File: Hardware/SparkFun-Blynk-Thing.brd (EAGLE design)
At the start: 50.2 x 41.9 mm, 100 parts, among them Q1 MMBT2222A, Q2 MMBT2222A, Q3 2.5A/30V, U2 ESP8266, U3 W25Q32FVSS, U4 FT231XS-U, U5 SI7021, U6 MCP73831, U7 AP2112K-3.3V, U8 OPAMP-DUALU, Y1 26MHz

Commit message: Schematic cleanup
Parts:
- removed C19: 2.2uF, SparkFun-Capacitors:0603-CAP
- removed D7: RED, SparkFun-LED:LED-0603
- removed J1, J10, J12, J5, J7, J8, J9: (no value), blynk-thing-temp:1X01_ALLIGATOR_3MM_HALF
- removed R22: 2.0k, SparkFun-Resistors:0603-RES
- removed R25: 22K, SparkFun-Resistors:0603-RES
- removed R26: 10K, SparkFun-Resistors:0603-RES
- removed U7: AP2112K-3.3V, SparkFun-PowerIC:SOT23-5
- added C5: 0.1uF, SparkFun-Capacitors:0603-CAP
- added D2: BAT20J, SparkFun-DiscreteSemi:SOD-323
- added JP19, JP21, JP23, JP25, JP27, JP28: (no value), SparkFun-Connectors:1X01_NO_SILK
- added JP29: (no value), SparkFun-Connectors:JST-4-PTH-VERT
- added R11: 330, SparkFun-Resistors:0603-RES
- added R13: 27, SparkFun-Resistors:0603-RES
- added R15: 4.7K, SparkFun-Resistors:0603-RES
- added U1: MCP73831, SparkFun-PowerIC:SOT23-5
- C10: value 0.1uF -> 2.2uF
- C11, C9: value 47pF -> 0.1uF
- C12: value 0.1uF -> 47pF
- C13: value 4.7uF -> 47pF
- C15: value 0.1uF -> 4.7uF
- C18: value 1.0uF -> 0.1uF; device SparkFun-Capacitors:0805-CAP -> SparkFun-Capacitors:0603-CAP
- C7: value 5.6pF -> 1.0uF; device SparkFun-Capacitors:0603-CAP -> SparkFun-Capacitors:0805-CAP
- C8: value 0.1uF -> 5.6pF
- D3: value (none) -> BLUE; device SparkFun-LED:WS2812B -> SparkFun-LED:LED-0603
- D4: value BLUE -> (none); device SparkFun-LED:LED-0603 -> SparkFun-LED:WS2812B
- D5: value BAT20J -> RED; device SparkFun-DiscreteSemi:SOD-323 -> SparkFun-LED:LED-0603
- JP1: value (none) -> LiPo; device SparkFun-Connectors:USB-B-MICRO-SMD_V03 -> SparkFun-Connectors:JST-2-PTH
- JP10, JP12, JP16, JP4, JP6, JP8: device SparkFun-Connectors:1X01_NO_SILK -> blynk-thing-temp:1X01_ALLIGATOR_3MM_HALF
- JP13: value LiPo -> (none); device SparkFun-Connectors:JST-2-PTH -> SparkFun-Connectors:1X01_NO_SILK
- JP14: device SparkFun-Connectors:1X01_NO_SILK -> SparkFun-Connectors:JST-3-PTH-VERT
- JP15: device SparkFun-Connectors:1X01_NO_SILK -> SparkFun-Connectors:USB-B-MICRO-SMD_V03
- JP2: device SparkFun-Connectors:JST-4-PTH-VERT -> blynk-thing-temp:1X01_ALLIGATOR_3MM_HALF
- JP3: device SparkFun-Connectors:JST-3-PTH-VERT -> SparkFun-Connectors:1X01_NO_SILK
- Q1: value MMBT2222A -> 2.5A/30V; device SparkFun-DiscreteSemi:SOT23-3@1 -> SparkFun-DiscreteSemi:SOT23-3
- Q3: value 2.5A/30V -> MMBT2222A; device SparkFun-DiscreteSemi:SOT23-3 -> SparkFun-DiscreteSemi:SOT23-3@1
- R14: value 10K -> 27; device SparkFun-Resistors:0603-RES@1 -> SparkFun-Resistors:0603-RES
- R16: value 330 -> 4.7K
- R18: value 4.7K -> 10K; device SparkFun-Resistors:0603-RES -> SparkFun-Resistors:0603-RES@1
- R2: value 10K -> 1K; device SparkFun-Resistors:0603-RES@1 -> SparkFun-Resistors:0603-RES
- R20: value 1K -> 10K; device SparkFun-Resistors:0603-RES -> SparkFun-Resistors:0603-RES@1
- R3: value DNP -> 22K; device SparkFun-Passives:1/6W-RES -> SparkFun-Resistors:0603-RES
- R4: value 200 -> 10K
- R5: value 10K -> DNP; device SparkFun-Resistors:0603-RES@1 -> SparkFun-Passives:1/6W-RES
- R6: value 4.7K -> 2.0k
- R7, R8: value 27 -> 10K; device SparkFun-Resistors:0603-RES -> SparkFun-Resistors:0603-RES@1
- R9: value 10K -> 200; device SparkFun-Resistors:0603-RES@1 -> SparkFun-Resistors:0603-RES
- SJ1: device SparkFun-Passives:PAD-JUMPER-3-NC_BY_PASTE_YES_SILK_FULL_BOX -> SparkFun-Passives:PAD-JUMPER-2-NC_BY_TRACE_YES_SILK
- SJ2: value (none) -> PWRLED
- SJ3: value PWRLED -> (none); device SparkFun-Passives:PAD-JUMPER-2-NC_BY_TRACE_YES_SILK -> SparkFun-Passives:PAD-JUMPER-3-NC_BY_PASTE_YES_SILK_FULL_BOX
- U3: value W25Q32FVSS -> AP2112K-3.3V; device blynk-thing-temp:SO08 -> SparkFun-PowerIC:SOT23-5
- U5: value SI7021 -> W25Q32FVSS; device SparkFun-Sensors:SI7021 -> blynk-thing-temp:SO08
- U6: value MCP73831 -> SI7021; device SparkFun-PowerIC:SOT23-5 -> SparkFun-Sensors:SI7021
- moved JP12 42.2 mm to (33.7, 2.54), turned to 180 degrees
- moved JP4 38.1 mm to (13.3, 2.54), turned to 180 degrees
- moved JP11 34.1 mm to (28.6, 5.71)
- moved JP10 34.0 mm to (28.6, 2.54), turned to 180 degrees
- moved JP6 33.7 mm to (18.4, 2.54), turned to 180 degrees
- moved R16 32.8 mm to (8.89, 32.4), turned to 270 degrees
- moved C8 31.2 mm to (37.5, 22.9), turned to 0 degrees
- moved JP9 30.9 mm to (23.5, 5.71)
- moved JP17 30.5 mm to (8.26, 36.2)
- moved R19 30.1 mm to (34.3, 32.4), turned to 270 degrees
- moved R2 30.1 mm to (9.53, 10.8), turned to 270 degrees
- moved R18 29.6 mm to (29.8, 11.4), turned to 0 degrees
- moved JP2 29.1 mm to (8.26, 2.54), turned to 180 degrees
- moved JP3 28.9 mm to (8.26, 5.71)
- moved JP13 28.0 mm to (33.7, 5.71), turned to 0 degrees
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- renumbered C20 to C6, D6 to D1, J11 to JP26, J2 to JP18, J3 to JP22, J4 to JP24, J6 to JP20, R21 to R12, U8 to IC1
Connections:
- net 0/BUTTON: now also JP27.1, Q3.3, R19.1; no longer JP16.1, Q2.3, R14.1
- net 14/SCL: now also JP29.4, R16.1, U6.SCK; no longer JP2.4, R18.1, U5.SCK
- net 2/SDA: now also JP29.3, R15.1, U6.DATA; no longer JP2.3, R6.1, U5.DATA
- net 3.3V_F: now also C16.1; no longer C14.1
- net 4/WS2812: now also D4.4; no longer D3.4
- net ADC-IN: now also JP21.1; no longer JP6.1
- net CHIP_EN: now also R8.1; no longer R2.1
- net D+: now also C13.1, JP15.D+1, R14.1; no longer C11.1, JP1.D+1, R8.1
- net D-: now also C12.1, JP15.D-1, R13.1; no longer C9.1, JP1.D-1, R7.1
- net DTR: now also Q3.2, R17.1; no longer Q2.2, R9.1
- net GND: now also C5.2, C7.2, D4.3, JP1.1, JP14.2, JP15.GND1, JP29.1, JP6.1@2, JP7.1, R11.2, R20.1, R4.1, R5.1, R6.1, R7.1, SJ2.1, U1.2, U3.2, U5.4, U6.GND; no longer C19.2, C8.2, D3.3, J8.1@2, JP1.GND1, JP13.1, JP2.1, JP3.2, JP8.1, R16.2, R17.1, R19.1, R22.1, R26.1, R3.1, SJ3.1, U3.4, U5.GND, U6.2, U7.2
- net GPIO12: now also JP16.1@2, JP17.1; no longer J1.1@2, JP12.1
- net GPIO13: now also JP19.1; no longer JP11.1
- net GPIO15: now also JP23.1, R20.2; no longer JP10.1, R17.2
- net GPIO16: now also JP25.1; no longer JP9.1
- net GPIO5: now also D3.A, JP12.1@2, JP13.1; no longer D4.A, J5.1@2, JP5.1
- net LNA: now also C8.1; no longer C7.1
- net N$10: now also D5.A; no longer D7.A
- net N$11: now also R15.2, SJ3.3; no longer R6.2, SJ1.3
- net N$12: now also Q3.1, R18.2; no longer Q2.1, R10.2
- net N$13: now also R16.2, SJ3.1; no longer R18.2, SJ1.1
- net N$14: now also R5.2, SJ1.2, U1.5; no longer R3.2, SJ2.2, U6.5
- net N$15: now also R3.2; no longer R25.2
- net N$16: now also R6.2, SJ1.1; no longer R22.2, SJ2.1
- net N$17: now also R2.2; no longer R20.2
- net N$18: now also R3.1, R4.2; no longer R25.1, R26.2
- net N$4: now also R13.2; no longer R7.2
- net N$5: now also D5.C, SJ2.2; no longer D7.C, SJ3.2
- net N$6: now also Q2.1, R17.2; no longer Q1.1, R9.2
- net N$7: now also R14.2; no longer R8.2
- net N$8: now also D3.C, R11.1; no longer D4.C, R16.1
- net N$9: now also R2.1, U1.1; no longer R20.1, U6.1
- net RESET: now also JP28.1, Q2.3, R10.1; no longer JP4.1, Q1.3, R5.1
- net RTS: now also Q2.2, R18.1; no longer Q1.2, R10.1
- net SD_!HD!: now also U5.7; no longer U3.7
- net SD_!WP!: now also U5.3; no longer U3.3
- net SD_CLK: now also R9.1, U5.6; no longer R4.1, U3.6
- net SD_CLK0: now also R9.2; no longer R4.2
- net SD_CS0: now also U5.1; no longer U3.1
- net SD_SI: now also U5.5; no longer U3.5
- net SD_SO: now also U5.2; no longer U3.2
- net SHIELD: now also JP15.SHIELD1, JP15.SHIELD2, JP15.SHIELD3; no longer JP1.SHIELD1, JP1.SHIELD2, JP1.SHIELD3
- net TRACE_ANT: now also C8.2; no longer C7.2
- net U0RXI: now also JP8.1@2, JP9.1; no longer J10.1@2, JP15.1
- net U0TXO: now also JP10.1@2, JP11.1; no longer J9.1@2, JP14.1
- net VBAT: now also JP1.2, Q1.3, U1.3; no longer JP13.2, Q3.3, U6.3
- net VCC: now also C18.1, C5.1, C9.1, D4.1, JP14.1, JP29.2, JP4.1@2, JP5.1, R10.2, R19.2, R8.2, SJ3.2, U3.5, U5.8, U6.VDD; no longer C15.1, C16.1, C19.1, D3.1, J7.1@2, JP2.2, JP3.1, JP7.1, R14.2, R2.2, R5.2, SJ1.2, U3.8, U5.VDD, U7.5
- net VIN: now also C7.1, D2.C, JP2.1@2, JP3.1, Q1.2, U3.1, U3.3; no longer C18.1, D5.C, J12.1@2, JP17.1, Q3.2, U7.1, U7.3
- net VUSB: now also C11.1, JP15.VBUS1; no longer C8.1, JP1.VBUS1
- net V_USB: now also C14.1, C15.1, D2.A, Q1.1, R7.2, U1.4; no longer C12.1, C13.1, D5.A, Q3.1, R19.2, U6.4
- net WS2812-DOUT: now also D4.2, JP14.3; no longer D3.2, JP3.3

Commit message: Board cleanup
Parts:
- U2: device esp8266-development-board:QFN32 -> SparkFun-RF:QFN32
- moved D1 0.64 mm to (2.54, 8.26)
- moved D5 0.64 mm to (2.54, 6.35)
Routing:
- net V_USB: track 58.7 -> 58.0 mm
- net N$10: track 8.37 -> 7.73 mm
- net N$17: track 9.73 -> 9.09 mm
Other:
- board text added: "3V3"
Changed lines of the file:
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@@
 <layer number="47" name="Measures" color="7" fill="1" visible="no" active="yes"/>
 <layer number="48" name="Document" color="7" fill="1" visible="no" active="yes"/>
-<layer number="49" name="Reference" color="7" fill="1" visible="no" active="yes"/>
+<layer number="49" name="Reference" color="7" fill="1" visible="yes" active="yes"/>
 <layer number="50" name="dxf" color="7" fill="1" visible="no" active="no"/>
 <layer number="51" name="tDocu" color="6" fill="1" visible="yes" active="yes"/>
@@
 <text x="18.542" y="6.858" size="1.27" layer="21" ratio="15" align="bottom-center">GND</text>
 <text x="47.625" y="22.86" size="1.778" layer="21" ratio="15" rot="R90" align="top-center">Blynk Thing</text>
-<text x="3.4925" y="6.35" size="1.016" layer="21" font="vector" ratio="15" align="center-left">PWR</text>
-<text x="3.4925" y="8.255" size="1.016" layer="21" font="vector" ratio="15" align="center-left">CHG</text>
+<text x="4.1275" y="6.35" size="1.016" layer="21" font="vector" ratio="15" align="center-left">PWR</text>
+<text x="4.1275" y="8.255" size="1.016" layer="21" font="vector" ratio="15" align="center-left">CHG</text>
 <text x="18.542" y="35.1155" size="1.27" layer="21" ratio="15" align="top-center">ADC</text>
 <text x="28.702" y="6.858" size="1.27" layer="21" ratio="15" align="bottom-center">TX</text>
@@
 <wire x1="29.718" y1="36.195" x2="29.972" y2="36.195" width="0.508" layer="22"/>
 <text x="6.604" y="36.195" size="1.016" layer="16" font="vector" ratio="15" rot="MR0">vSecret</text>
+<text x="1.953" y="35.052" size="0.8128" layer="21" font="vector" ratio="15" align="bottom-center">GND</text>
+<text x="3.048" y="32.369" size="0.8128" layer="21" font="vector" ratio="15" rot="R270" align="bottom-center">3V3</text>
+<text x="3.048" y="29.861" size="0.8128" layer="21" font="vector" ratio="15" rot="R270" align="bottom-center">SDA</text>
+<text x="2.207" y="27.178" size="0.8128" layer="21" font="vector" ratio="15" rot="R180" align="bottom-center">SCL</text>
 </plain>
 <attributes>
@@
 <element name="STANDOFF3" library="SparkFun-Electromechanical" package="STAND-OFF" value="STAND-OFF" x="39.37" y="39.37"/>
 <element name="STANDOFF4" library="SparkFun-Electromechanical" package="STAND-OFF" value="STAND-OFF" x="39.37" y="2.54"/>
-<element name="U2" library="esp8266-development-board" package="QFN32" value="ESP8266" x="30.48" y="24.13" rot="R180">
+<element name="U2" library="SparkFun-RF" package="QFN32" value="ESP8266" x="30.48" y="24.13" rot="R180">
 <attribute name="PROD_ID" value="IC-12452" x="30.48" y="24.13" size="1.778" layer="27" rot="R180" display="off"/>
 </element>
@@
 <attribute name="PROD_ID" value="CONN-09863" x="7.62" y="-5.715" size="1.778" layer="27" font="vector" ratio="15" rot="R90" display="off"/>
 </element>
-<element name="D1" library="SparkFun-LED" package="LED-0603" value="Yellow" x="1.905" y="8.255" rot="R270">
-<attribute name="PROD_ID" value="DIO-09003" x="8.255" y="33.655" size="1.778" layer="27" font="vector" ratio="15" rot="R270" display="off"/>
+<element name="D1" library="SparkFun-LED" package="LED-0603" value="Yellow" x="2.54" y="8.255" rot="R270">
+<attribute name="PROD_ID" value="DIO-09003" x="8.89" y="33.655" size="1.778" layer="27" font="vector" ratio="15" rot="R270" display="off"/>
 </element>
 <element name="R2" library="SparkFun-Resistors" package="0603-RES" value="1K" x="9.525" y="10.795" rot="R270">
@@
 <attribute name="PROD_ID" value="RES-07856" x="12.065" y="-36.83" size="1.778" layer="27" font="vector" ratio="15" rot="R90" display="off"/>
 </element>
-<element name="D5" library="SparkFun-LED" package="LED-0603" value="RED" x="1.905" y="6.35" rot="R90">
-<attribute name="PROD_ID" value="DIO-00819" x="8.255" y="-34.29" size="1.778" layer="27" font="vector" ratio="15" rot="R90" display="off"/>
+<element name="D5" library="SparkFun-LED" package="LED-0603" value="RED" x="2.54" y="6.35" rot="R90">
+<attribute name="PROD_ID" value="DIO-00819" x="8.89" y="-34.29" size="1.778" layer="27" font="vector" ratio="15" rot="R90" display="off"/>
 </element>
 <element name="R6" library="SparkFun-Resistors" package="0603-RES" value="2.0k" x="13.335" y="12.065">
@@
 <wire x1="14.92" y1="15.605" x2="13.92" y2="14.605" width="0.4064" layer="1"/>
 <wire x1="14.92" y1="15.605" x2="16.24" y2="15.605" width="0.4064" layer="1"/>
-<wire x1="1.028" y1="8.255" x2="1.028" y2="13.093" width="0.254" layer="1"/>
-<wire x1="1.028" y1="13.093" x2="2.54" y2="14.605" width="0.254" layer="1"/>
+<wire x1="1.663" y1="8.255" x2="1.663" y2="13.093" width="0.254" layer="1"/>
+<wire x1="1.663" y1="13.093" x2="3.175" y2="14.605" width="0.254" layer="1"/>
 <wire x1="15.2701" y1="8.575" x2="16.195" y2="8.575" width="0.4064" layer="1"/>
 <wire x1="16.5575" y1="15.2875" x2="16.24" y2="15.605" width="0.4064" layer="1"/>
@@
 <wire x1="7.366" y1="17.145" x2="7.366" y2="14.605" width="0.4064" layer="1"/>
 <wire x1="7.366" y1="14.605" x2="7.405" y2="14.605" width="0.4064" layer="1"/>
-<wire x1="7.366" y1="14.605" x2="2.54" y2="14.605" width="0.254" layer="1"/>
+<wire x1="7.366" y1="14.605" x2="3.175" y2="14.605" width="0.254" layer="1"/>
 <wire x1="7.405" y1="14.605" x2="8.04" y2="13.97" width="0.4064" layer="1"/>
 <wire x1="8.04" y1="13.97" x2="8.675" y2="13.97" width="0.4064" layer="1"/>
@@
 <wire x1="9.525" y1="9.945" x2="10.248" y2="9.945" width="0.2032" layer="1"/>
 <wire x1="10.248" y1="9.945" x2="10.668" y2="9.525" width="0.2032" layer="1"/>
-<wire x1="2.782" y1="8.255" x2="4.445" y2="8.255" width="0.254" layer="1"/>
+<wire x1="3.417" y1="8.255" x2="4.445" y2="8.255" width="0.254" layer="1"/>
 <wire x1="4.445" y1="8.255" x2="5.08" y2="8.89" width="0.254" layer="1"/>
 <wire x1="5.08" y1="8.89" x2="7.62" y2="8.89" width="0.254" layer="1"/>
@@
 <contactref element="D5" pad="C"/>
 <contactref element="SJ2" pad="2"/>
-<wire x1="1.028" y1="6.35" x2="1.028" y2="5.092" width="0.2032" layer="1"/>
-<wire x1="1.028" y1="5.092" x2="0.889" y2="4.953" width="0.2032" layer="1"/>
+<wire x1="1.663" y1="6.35" x2="1.663" y2="5.727" width="0.2032" layer="1"/>
+<wire x1="1.663" y1="5.727" x2="0.889" y2="4.953" width="0.2032" layer="1"/>
 <via x="0.889" y="4.953" extent="1-16" drill="0.381"/>
 <wire x1="0.889" y1="4.953" x2="1.397" y2="5.461" width="0.2032" layer="16"/>
@@
 <contactref element="D5" pad="A"/>
 <contactref element="R12" pad="2"/>
-<wire x1="2.782" y1="6.35" x2="4.445" y2="6.35" width="0.254" layer="1"/>
+<wire x1="3.417" y1="6.35" x2="4.445" y2="6.35" width="0.254" layer="1"/>
 <wire x1="4.445" y1="6.35" x2="5.295" y2="7.2" width="0.254" layer="1"/>
 <wire x1="5.295" y1="7.2" x2="10.795" y2="7.2" width="0.254" layer="1"/>

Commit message: Adding dimensions
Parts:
- moved FRAME1 10.6 mm to (-5.71, -22.2)
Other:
- board text added: "Jim Lindblom"
- board text added: "Units in inches"
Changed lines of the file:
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@@
 <text x="3.048" y="29.861" size="0.8128" layer="21" font="vector" ratio="15" rot="R270" align="bottom-center">SDA</text>
 <text x="2.207" y="27.178" size="0.8128" layer="21" font="vector" ratio="15" rot="R180" align="bottom-center">SCL</text>
+<dimension x1="0" y1="2.54" x2="50.165" y2="8.255" x3="25.0825" y3="-11.43" textsize="0.762" textratio="15" layer="47" dtype="horizontal" unit="inch" precision="3"/>
+<dimension x1="0" y1="2.54" x2="41.91" y2="6.35" x3="20.955" y3="-9.525" textsize="0.762" textratio="15" layer="47" dtype="horizontal" unit="inch" precision="3"/>
+<dimension x1="0" y1="2.54" x2="39.37" y2="2.54" x3="19.685" y3="-7.62" textsize="0.762" textratio="15" layer="47" dtype="horizontal" unit="inch" precision="3"/>
+<dimension x1="0" y1="2.54" x2="33.655" y2="5.715" x3="16.8275" y3="-5.715" textsize="0.762" textratio="15" layer="47" dtype="horizontal" unit="inch" precision="3"/>
+<dimension x1="0" y1="2.54" x2="28.575" y2="5.715" x3="14.2875" y3="-3.81" textsize="0.762" textratio="15" layer="47" dtype="horizontal" unit="inch" precision="3"/>
+<dimension x1="0" y1="2.54" x2="2.54" y2="2.54" x3="1.27" y3="-1.27" textsize="0.762" textratio="15" layer="47" dtype="horizontal" unit="inch" precision="3"/>
+<dimension x1="2.54" y1="0" x2="2.54" y2="2.54" x3="-1.27" y3="1.27" textsize="0.762" textratio="15" layer="47" dtype="vertical" unit="inch" precision="3"/>
+<dimension x1="2.54" y1="0" x2="8.255" y2="5.715" x3="-4.445" y3="2.8575" textsize="0.762" textratio="15" layer="47" dtype="vertical" unit="inch" precision="3"/>
+<dimension x1="2.54" y1="0" x2="8.255" y2="36.195" x3="-10.16" y3="18.0975" textsize="0.762" textratio="15" layer="47" dtype="vertical" unit="inch" precision="3"/>
+<dimension x1="2.54" y1="0" x2="2.54" y2="39.37" x3="-12.065" y3="19.685" textsize="0.762" textratio="15" layer="47" dtype="vertical" unit="inch" precision="3"/>
+<dimension x1="2.54" y1="0" x2="3.175" y2="41.91" x3="-13.335" y3="20.955" textsize="0.762" textratio="15" layer="47" dtype="vertical" unit="inch" precision="3"/>
+<dimension x1="2.54" y1="0" x2="46.355" y2="7.62" x3="-6.35" y3="3.81" textsize="0.762" textratio="15" layer="47" dtype="vertical" unit="inch" precision="3"/>
+<dimension x1="2.54" y1="0" x2="46.355" y2="34.29" x3="-8.89" y3="17.145" textsize="0.762" textratio="15" layer="47" dtype="vertical" unit="inch" precision="3"/>
+<text x="-12.065" y="-5.08" size="0.762" layer="47" font="vector" ratio="15" align="center-left">Units in inches</text>
+<text x="24.765" y="-22.225" size="1.778" layer="51" font="vector" ratio="15">Jim Lindblom</text>
 </plain>
 <attributes>
@@
 </element>
 <element name="SJ2" library="SparkFun-Passives" package="PAD-JUMPER-2-NC_BY_TRACE_YES_SILK" value="PWRLED" x="1.905" y="6.35" rot="MR0"/>
-<element name="FRAME1" library="SparkFun-Aesthetics" package="CREATIVE_COMMONS" value="FRAME-LEDGER" x="0" y="-13.335"/>
+<element name="FRAME1" library="SparkFun-Aesthetics" package="CREATIVE_COMMONS" value="FRAME-LEDGER" x="-5.715" y="-22.225"/>
 <element name="JP28" library="SparkFun-Connectors" package="1X01_NO_SILK" value="" x="31.115" y="36.195"/>
 <element name="R5" library="SparkFun-Passives" package="1/6W-RES" value="DNP" x="13.335" y="12.065" smashed="yes">

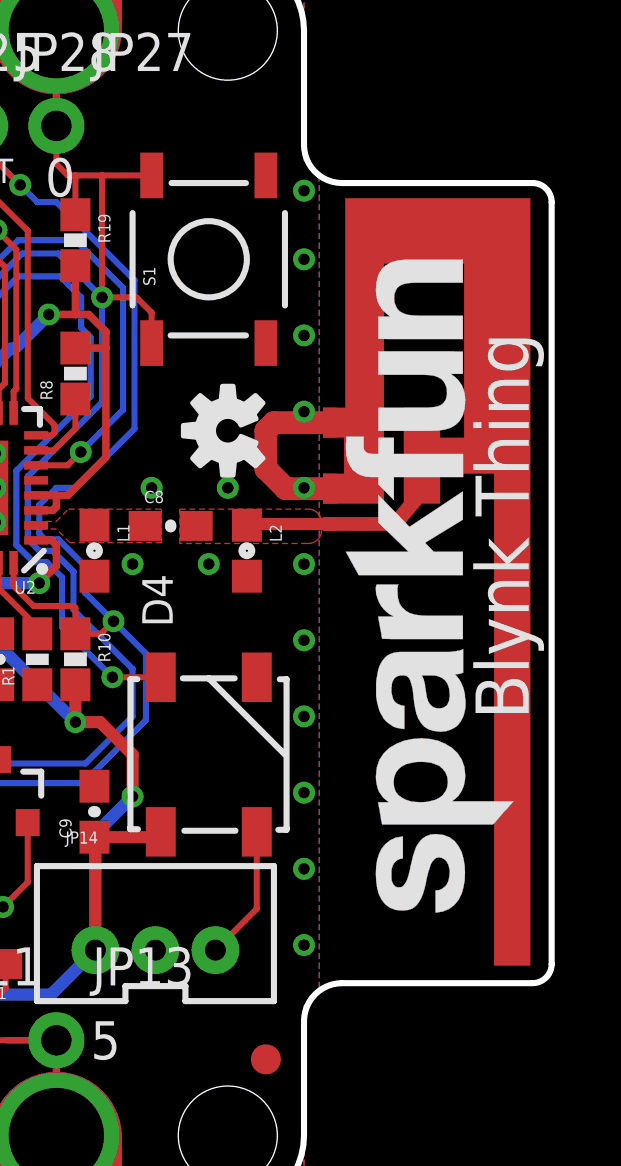
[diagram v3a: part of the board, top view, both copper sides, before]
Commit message: Adjsting board dimension to 0.01in grid
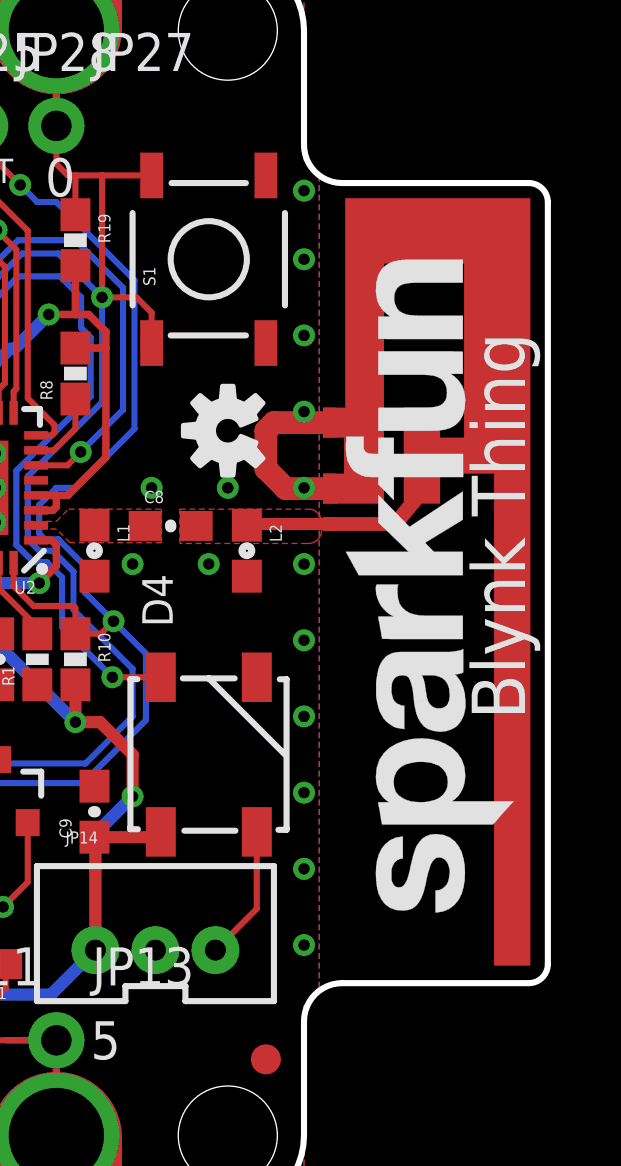
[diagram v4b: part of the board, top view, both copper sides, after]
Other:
- board size 50.2 x 41.9 mm -> 50 x 41.9 mm
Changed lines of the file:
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@@
 <text x="13.462" y="6.858" size="1.2065" layer="21" ratio="15" align="bottom-center">3.3V</text>
 <text x="18.542" y="6.858" size="1.27" layer="21" ratio="15" align="bottom-center">GND</text>
-<text x="47.625" y="22.86" size="1.778" layer="21" ratio="15" rot="R90" align="top-center">Blynk Thing</text>
+<text x="47.498" y="22.86" size="1.778" layer="21" ratio="15" rot="R90" align="top-center">Blynk Thing</text>
 <text x="4.1275" y="6.35" size="1.016" layer="21" font="vector" ratio="15" align="center-left">PWR</text>
 <text x="4.1275" y="8.255" size="1.016" layer="21" font="vector" ratio="15" align="center-left">CHG</text>
@@
 <wire x1="41.91" y1="39.37" x2="41.91" y2="35.56" width="0.2032" layer="20"/>
 <wire x1="41.91" y1="35.56" x2="43.18" y2="34.29" width="0.2032" layer="20" curve="90"/>
-<wire x1="43.18" y1="34.29" x2="49.53" y2="34.29" width="0.2032" layer="20"/>
-<wire x1="49.53" y1="34.29" x2="50.165" y2="33.655" width="0.2032" layer="20" curve="-90"/>
-<wire x1="50.165" y1="33.655" x2="50.165" y2="8.255" width="0.2032" layer="20"/>
-<wire x1="50.165" y1="8.255" x2="49.53" y2="7.62" width="0.2032" layer="20" curve="-90"/>
-<wire x1="49.53" y1="7.62" x2="43.18" y2="7.62" width="0.2032" layer="20"/>
+<wire x1="43.18" y1="34.29" x2="49.403" y2="34.29" width="0.2032" layer="20"/>
+<wire x1="49.403" y1="34.29" x2="50.038" y2="33.655" width="0.2032" layer="20" curve="-90"/>
+<wire x1="50.038" y1="33.655" x2="50.038" y2="8.255" width="0.2032" layer="20"/>
+<wire x1="50.038" y1="8.255" x2="49.403" y2="7.62" width="0.2032" layer="20" curve="-90"/>
+<wire x1="49.403" y1="7.62" x2="43.18" y2="7.62" width="0.2032" layer="20"/>
 <wire x1="43.18" y1="7.62" x2="41.91" y2="6.35" width="0.2032" layer="20" curve="90"/>
 <wire x1="41.91" y1="6.35" x2="41.91" y2="2.54" width="0.2032" layer="20"/>
@@
 <text x="3.048" y="29.861" size="0.8128" layer="21" font="vector" ratio="15" rot="R270" align="bottom-center">SDA</text>
 <text x="2.207" y="27.178" size="0.8128" layer="21" font="vector" ratio="15" rot="R180" align="bottom-center">SCL</text>
-<dimension x1="0" y1="2.54" x2="50.165" y2="8.255" x3="25.0825" y3="-11.43" textsize="0.762" textratio="15" layer="47" dtype="horizontal" unit="inch" precision="3"/>
+<dimension x1="0" y1="2.54" x2="50.038" y2="8.255" x3="25.019" y3="-11.43" textsize="0.762" textratio="15" layer="47" dtype="horizontal" unit="inch" precision="3"/>
 <dimension x1="0" y1="2.54" x2="41.91" y2="6.35" x3="20.955" y3="-9.525" textsize="0.762" textratio="15" layer="47" dtype="horizontal" unit="inch" precision="3"/>
 <dimension x1="0" y1="2.54" x2="39.37" y2="2.54" x3="19.685" y3="-7.62" textsize="0.762" textratio="15" layer="47" dtype="horizontal" unit="inch" precision="3"/>
